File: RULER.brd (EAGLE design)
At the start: 180 x 22 mm, 0 parts

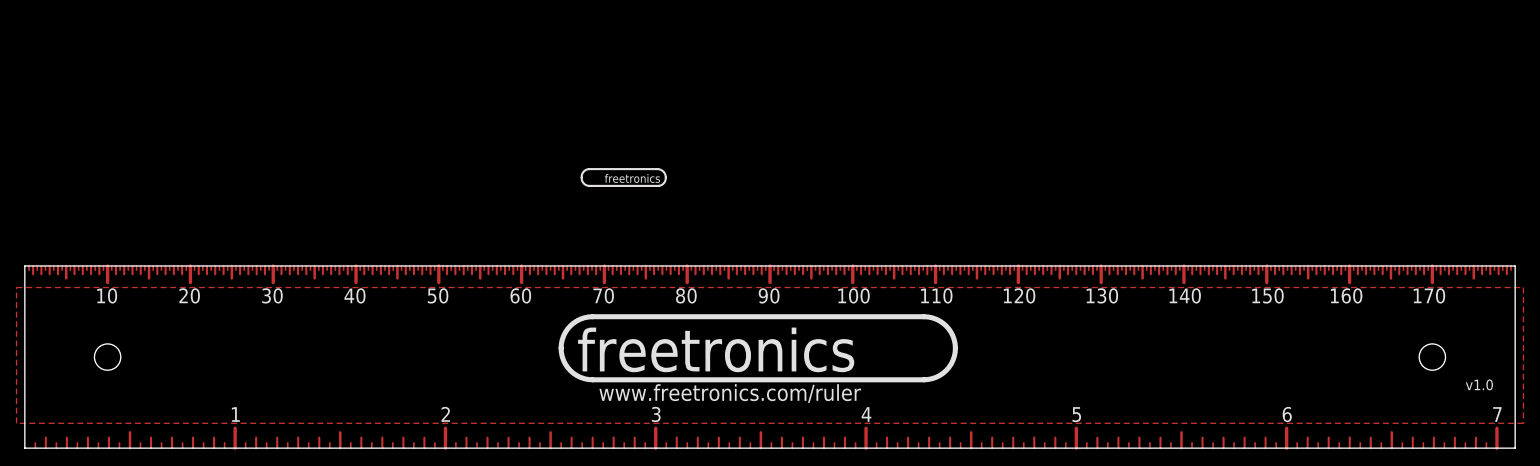
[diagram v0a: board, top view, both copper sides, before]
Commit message: Added info tables to top
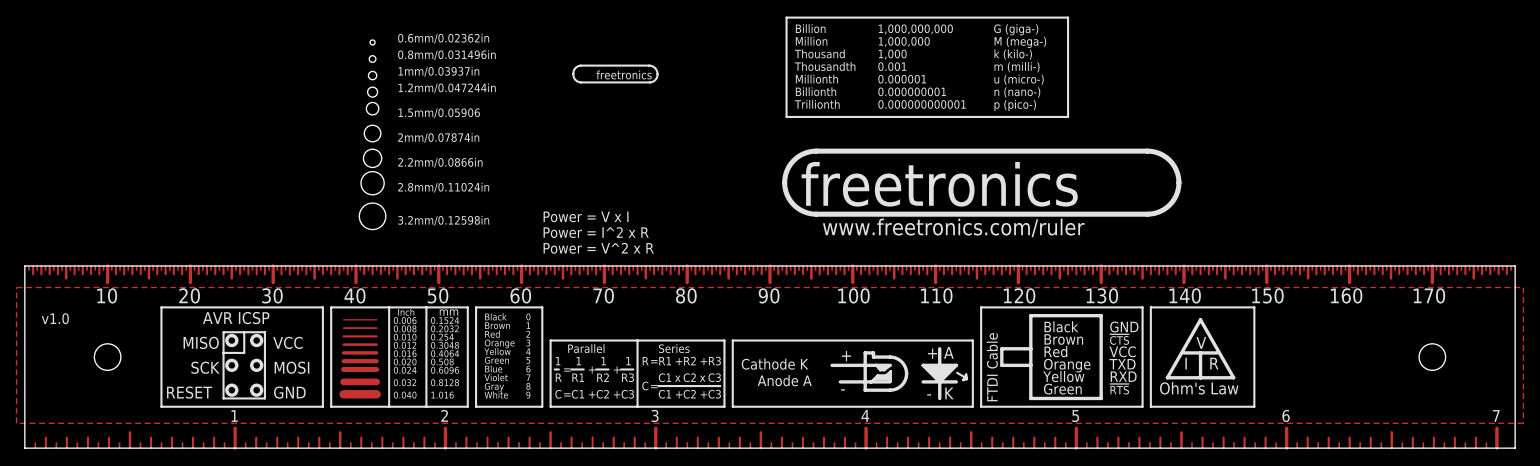
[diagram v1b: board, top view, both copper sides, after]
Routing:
- net N$509: track 0.00 -> 4.00 mm
- net N$508: track 0.00 -> 4.00 mm
- net N$507: track 0.00 -> 4.00 mm
- net N$506: track 0.00 -> 4.00 mm
- net N$505: track 0.00 -> 4.00 mm
- net N$504: track 0.00 -> 4.00 mm
- net N$503: track 0.00 -> 4.00 mm
- net N$502: track 0.00 -> 4.00 mm
- net N$501: track 0.00 -> 4.00 mm
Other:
- board text added: "!CTS"
- board text added: "!RTS"
- board text added: "+"
- board text added: "-"
- board text added: "0 1 2 3 4 5 6 7 8 9"
- board text added: "0.006"
- board text added: "0.008"
- board text added: "0.010"
- board text added: "0.012"
- board text added: "0.016"
- board text added: "0.020"
- board text added: "0.024"
- board text added: "0.032"
- board text added: "0.040"
- board text added: "0.1524"
- board text added: "0.2032"
- board text added: "0.254"
- board text added: "0.3048"
- board text added: "0.4064"
- board text added: "0.508"
- board text added: "0.6096"
- board text added: "0.6mm/0.02362in"
- board text added: "0.8128"
- board text added: "0.8mm/0.031496in"
- board text added: "1,000,000,000 1,000,000 1,000 0.001 0.000001 0.000000001 0.000000000001"
- board text added: "1.016"
- board text added: "1.2mm/0.047244in"
- board text added: "1.5mm/0.05906"
- board text added: "1mm/0.03937in"
- board text added: "2.2mm/0.0866in"
- board text added: "2.8mm/0.11024in"
- board text added: "2mm/0.07874in"
- board text added: "3.2mm/0.12598in"
- board text added: "="
- board text added: "AVR ICSP"
- board text added: "Anode A"
- board text added: "Billion Million Thousand Thousandth Millionth Billionth Trillionth"
- board text added: "Black"
- board text added: "Black Brown Red Orange Yellow Green Blue Violet Gray White"
- board text added: "Brown"
- board text added: "C"
- board text added: "C1"
- board text added: "C2"
- board text added: "C3"
- board text added: "Cathode K"
- board text added: "FTDI Cable"
- board text added: "G (giga-) M (mega-) k (kilo-) m (milli-) u (micro-) n (nano-) p (pico-)"
- board text added: "GND"
- board text added: "Green"
- board text added: "I"
- board text added: "Inch"
- board text added: "MISO"
- board text added: "MOSI"
- board text added: "Ohm's Law"
- board text added: "Orange"
- board text added: "Parallel"
- board text added: "Power = V x I Power = I^2 x R Power = V^2 x R"
- board text added: "R"
- board text added: "R1"
- board text added: "R2"
- board text added: "R3"
- board text added: "RESET"
- board text added: "RXD"
- board text added: "Red"
- board text added: "SCK"
- board text added: "Series"
- board text added: "TXD"
- board text added: "V"
- board text added: "VCC"
- board text added: "Yellow"
- board text added: "mm"
- board text added: "x"

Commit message: Removed 0.5mm marks
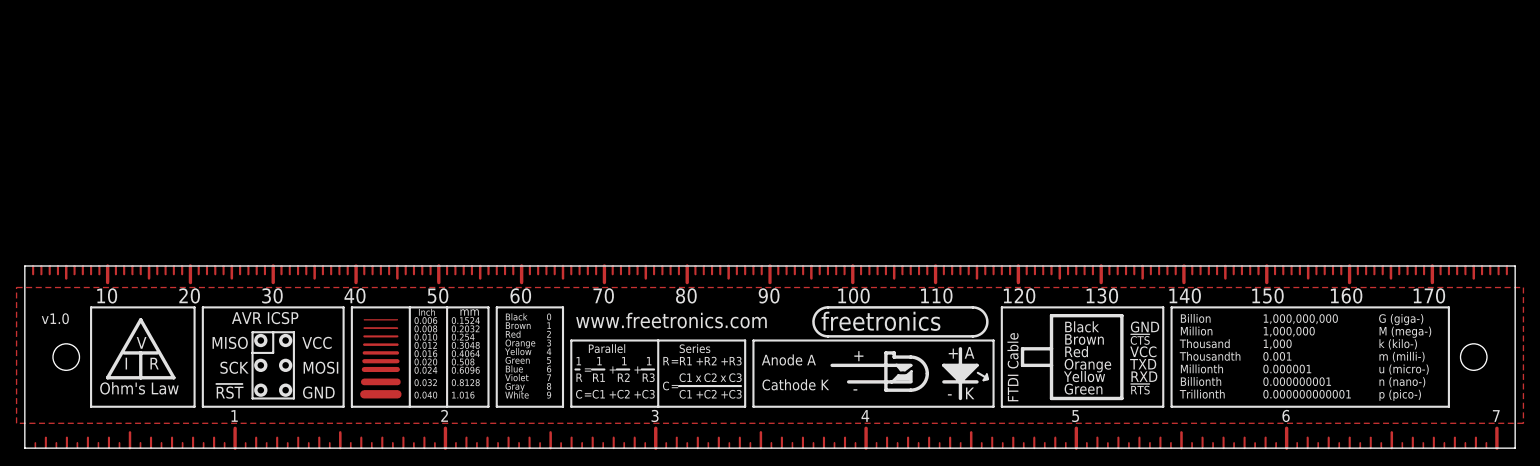
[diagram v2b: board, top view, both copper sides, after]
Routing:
- net N$90: track 0.50 -> 0.00 mm
- net N$89: track 0.50 -> 0.00 mm
- net N$88: track 0.50 -> 0.00 mm
- net N$87: track 0.50 -> 0.00 mm
- net N$86: track 0.50 -> 0.00 mm
- net N$85: track 0.50 -> 0.00 mm
- net N$84: track 0.50 -> 0.00 mm
- net N$83: track 0.50 -> 0.00 mm
- net N$82: track 0.50 -> 0.00 mm
- net N$81: track 0.50 -> 0.00 mm
- net N$71: track 0.50 -> 0.00 mm
- net N$70: track 0.50 -> 0.00 mm
- net N$69: track 0.50 -> 0.00 mm
- net N$68: track 0.50 -> 0.00 mm
- net N$67: track 0.50 -> 0.00 mm
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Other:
- board text added: "!RST"
- board text added: "www.freetronics.com"
- board text removed: "0.6mm/0.02362in"
- board text removed: "0.8mm/0.031496in"
- board text removed: "1.2mm/0.047244in"
- board text removed: "1.5mm/0.05906"
- board text removed: "1mm/0.03937in"
- board text removed: "2.2mm/0.0866in"
- board text removed: "2.8mm/0.11024in"
- board text removed: "2mm/0.07874in"
- board text removed: "3.2mm/0.12598in"
- board text removed: "Power = V x I Power = I^2 x R Power = V^2 x R"
- board text removed: "RESET"

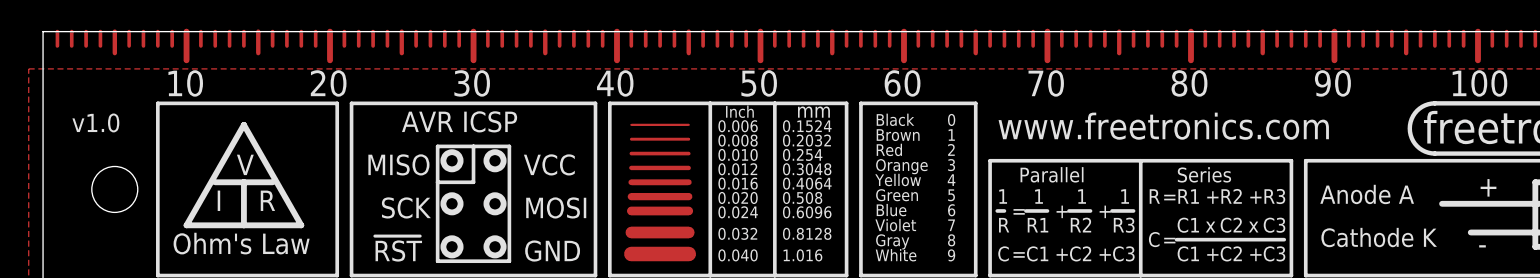
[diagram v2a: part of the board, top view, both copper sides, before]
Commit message: Changed silkscreen to fix URL
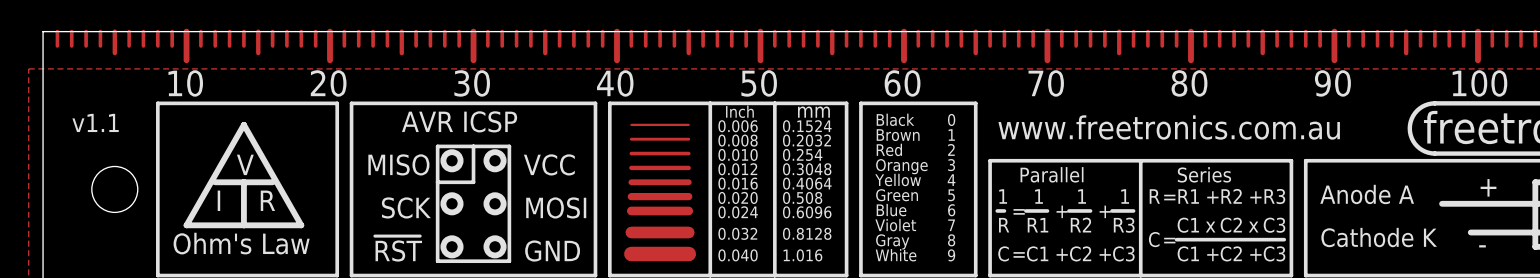
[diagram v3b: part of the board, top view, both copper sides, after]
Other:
- board text added: "v1.1"
- board text added: "www.freetronics.com.au"
- board text added: "www.freetronics.com.au/ruler"
- board text removed: "v1.0"
- board text removed: "www.freetronics.com"
- board text removed: "www.freetronics.com/ruler"
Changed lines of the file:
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@@
 <setting verticaltext="up"/>
 </settings>
-<grid distance="0.5" unitdist="mm" unit="mm" style="dots" multiple="1" display="yes" altdistance="0.005" altunitdist="inch" altunit="inch"/>
+<grid distance="1" unitdist="mm" unit="mm" style="dots" multiple="1" display="yes" altdistance="0.005" altunitdist="inch" altunit="inch"/>
 <layers>
 <layer number="1" name="Top" color="4" fill="1" visible="yes" active="yes"/>
@@
 <layer number="37" name="tTest" color="7" fill="1" visible="no" active="yes"/>
 <layer number="38" name="bTest" color="7" fill="1" visible="no" active="yes"/>
-<layer number="39" name="tKeepout" color="4" fill="11" visible="no" active="yes"/>
+<layer number="39" name="tKeepout" color="4" fill="11" visible="yes" active="yes"/>
 <layer number="40" name="bKeepout" color="1" fill="11" visible="no" active="yes"/>
 <layer number="41" name="tRestrict" color="4" fill="10" visible="yes" active="yes"/>
@@
 <text x="177.165" y="3.175" size="1.4224" layer="21" ratio="15">7</text>
 <hole x="5" y="11" drill="3.2"/>
-<text x="2" y="15" size="1.27" layer="21" ratio="15">v1.0</text>
+<text x="2" y="15" size="1.27" layer="21" ratio="15">v1.1</text>
 <circle x="28.5" y="13" radius="0.6" width="0.4064" layer="21"/>
 <circle x="28.5" y="10" radius="0.6" width="0.4064" layer="21"/>
@@
 <text x="52.5" y="16" size="1.016" layer="21" ratio="15">mm</text>
 <wire x1="46.5" y1="17" x2="46.5" y2="5" width="0.254" layer="21"/>
-<rectangle x1="40" y1="5.5" x2="46" y2="16.5" layer="41"/>
+<rectangle x1="40.2" y1="5.7" x2="45.8" y2="16.3" layer="29"/>
 <wire x1="27.5" y1="14" x2="30" y2="14" width="0.254" layer="21"/>
 <wire x1="30" y1="14" x2="32.5" y2="14" width="0.254" layer="21"/>
@@
 <wire x1="114.23" y1="12.065" x2="110.42" y2="8.255" width="0.6096" layer="22" curve="-90"/>
 <wire x1="110.42" y1="8.255" x2="70.415" y2="8.255" width="0.6096" layer="22"/>
-<text x="109.705" y="5.715" size="1.9304" layer="22" ratio="15" rot="MR0">www.freetronics.com/ruler</text>
+<text x="90" y="5.715" size="1.9304" layer="22" ratio="15" rot="MR0" align="bottom-center">www.freetronics.com.au/ruler</text>
 <text x="68" y="11.5" size="1.016" layer="21" ratio="12">Parallel</text>
 <text x="66.5" y="10" size="1.016" layer="21" ratio="12">1</text>
@@
 <wire x1="97" y1="17" x2="114.5" y2="17" width="0.3048" layer="21"/>
 <wire x1="114.5" y1="13.5" x2="97" y2="13.5" width="0.3048" layer="21"/>
-<text x="66.5" y="14.5" size="1.778" layer="21" ratio="15">www.freetronics.com</text>
+<text x="66.5" y="14.5" size="1.6" layer="21" ratio="15">www.freetronics.com.au</text>
+<rectangle x1="-1" y1="19.9" x2="181" y2="22" layer="29"/>
+<rectangle x1="-1" y1="0" x2="181" y2="2.5" layer="29"/>
+<rectangle x1="40" y1="5.5" x2="46" y2="16.5" layer="41"/>
 </plain>
 <attributes>
